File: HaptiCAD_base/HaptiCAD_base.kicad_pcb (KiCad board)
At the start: 4 copper layers, 170 x 110 mm, 99 parts, among them J101 BLDC, J301 USB_C_Receptacle_USB2.0_16P, J801 SWD, J802 Micro_SD_Card, U201 SN74LV1T34DBV, U401 MT6701CT, U402 VEML7700-TT, U501 AP2112K-3.3, U601 TMC6300-LA-T, U602 LMV321, U801 BMD-340-A-R, U802 ESD224DQA

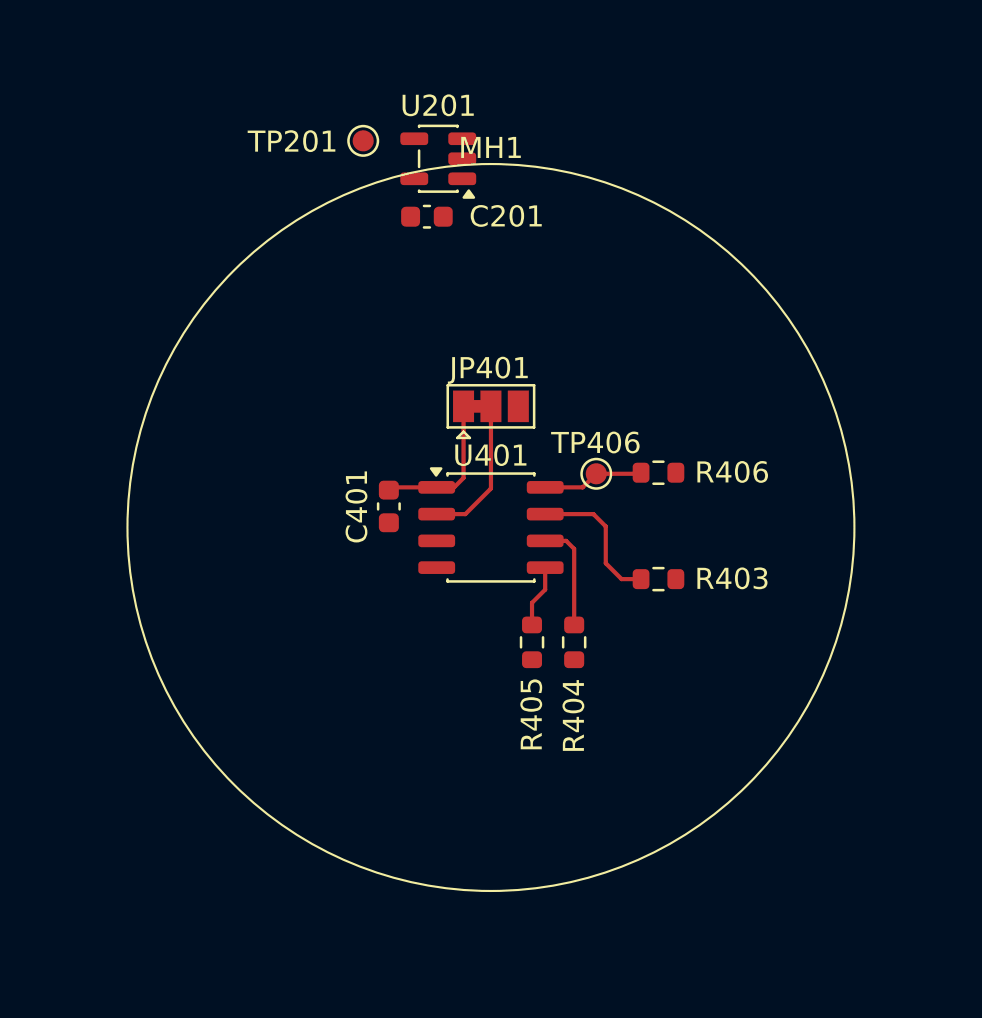
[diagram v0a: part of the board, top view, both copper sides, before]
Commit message: Split project into base and motor mount pcb
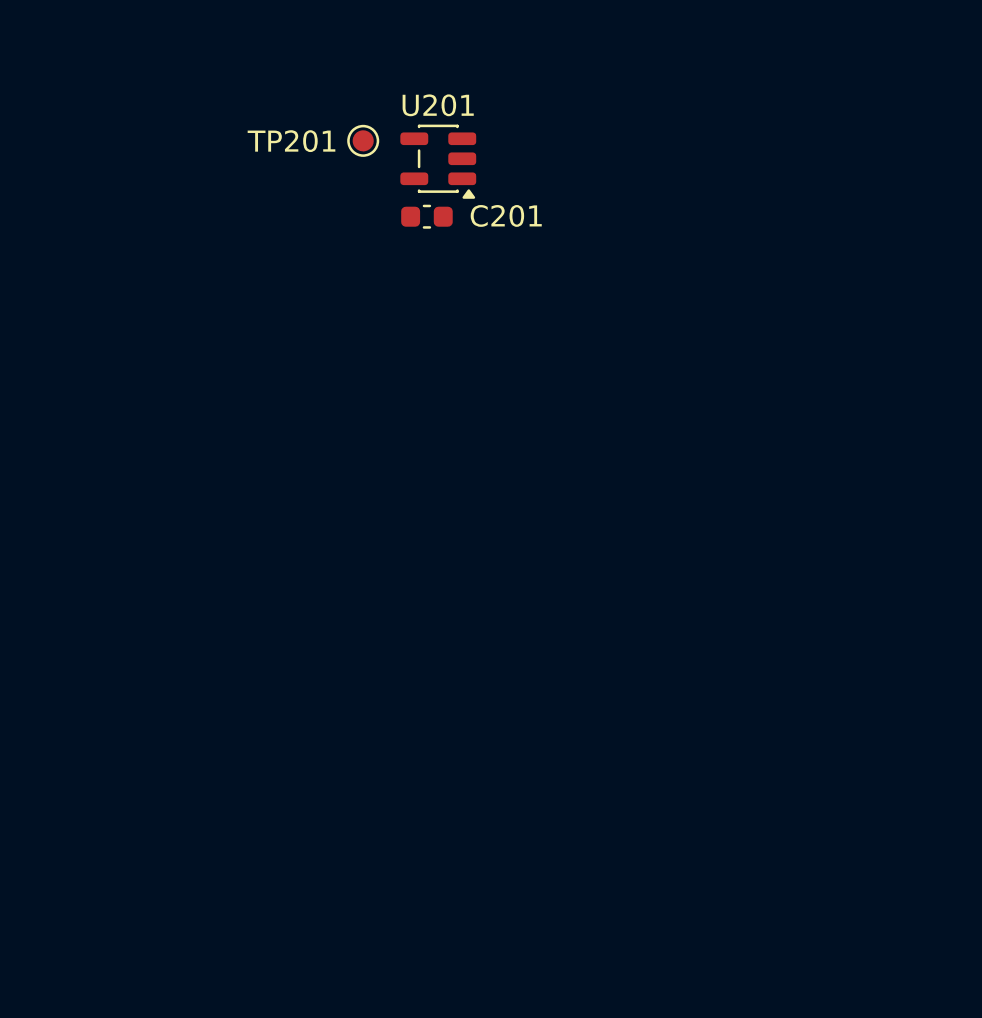
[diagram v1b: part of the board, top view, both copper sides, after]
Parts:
- removed C401: 0.1uF, Capacitor_SMD:C_0603_1608Metric
- removed JP401: SolderJumper_3_Bridged12, Jumper:SolderJumper-3_P1.3mm_Bridged12_Pad1.0x1.5mm
- removed MH1: ~, BLDC_mount:BLDC_mount
- removed R403, R404: 2.2k, Resistor_SMD:R_0603_1608Metric
- removed R405: 100k, Resistor_SMD:R_0603_1608Metric
- removed R406: 0, Resistor_SMD:R_0603_1608Metric
- removed TP406: ENC__~{CS}, TestPoint:TestPoint_Pad_D1.0mm
- removed U401: MT6701CT, Package_SO:SO-8_3.9x4.9mm_P1.27mm
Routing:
- net 5V: track 24.4 -> 17.2 mm
- net Net-(JP401-C): track 6.98 -> 0.00 mm
- net /Sensors/ENC_CLK: track 6.85 -> 0.00 mm
- net /Sensors/ENC_MISO: track 5.14 -> 0.00 mm
- net /Sensors/ENC__~{CS}: track 4.89 -> 0.00 mm
- net /Sensors/ENC__PUSH: track 2.98 -> 0.00 mm

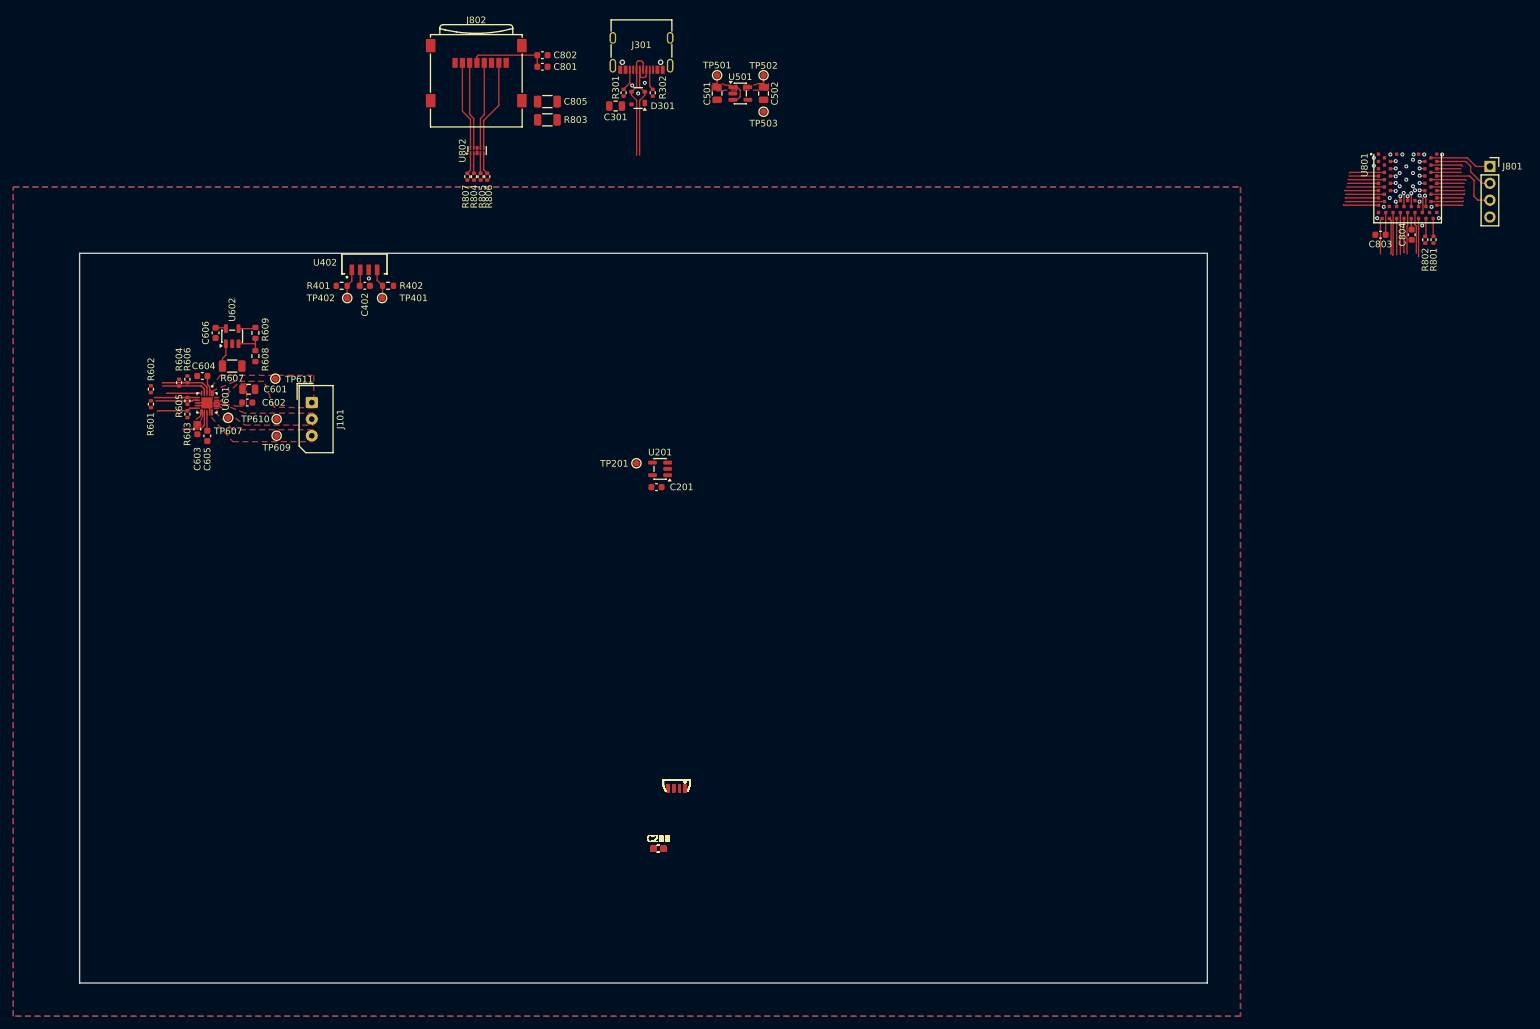
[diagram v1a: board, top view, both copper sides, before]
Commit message: updated base schematic and PCB
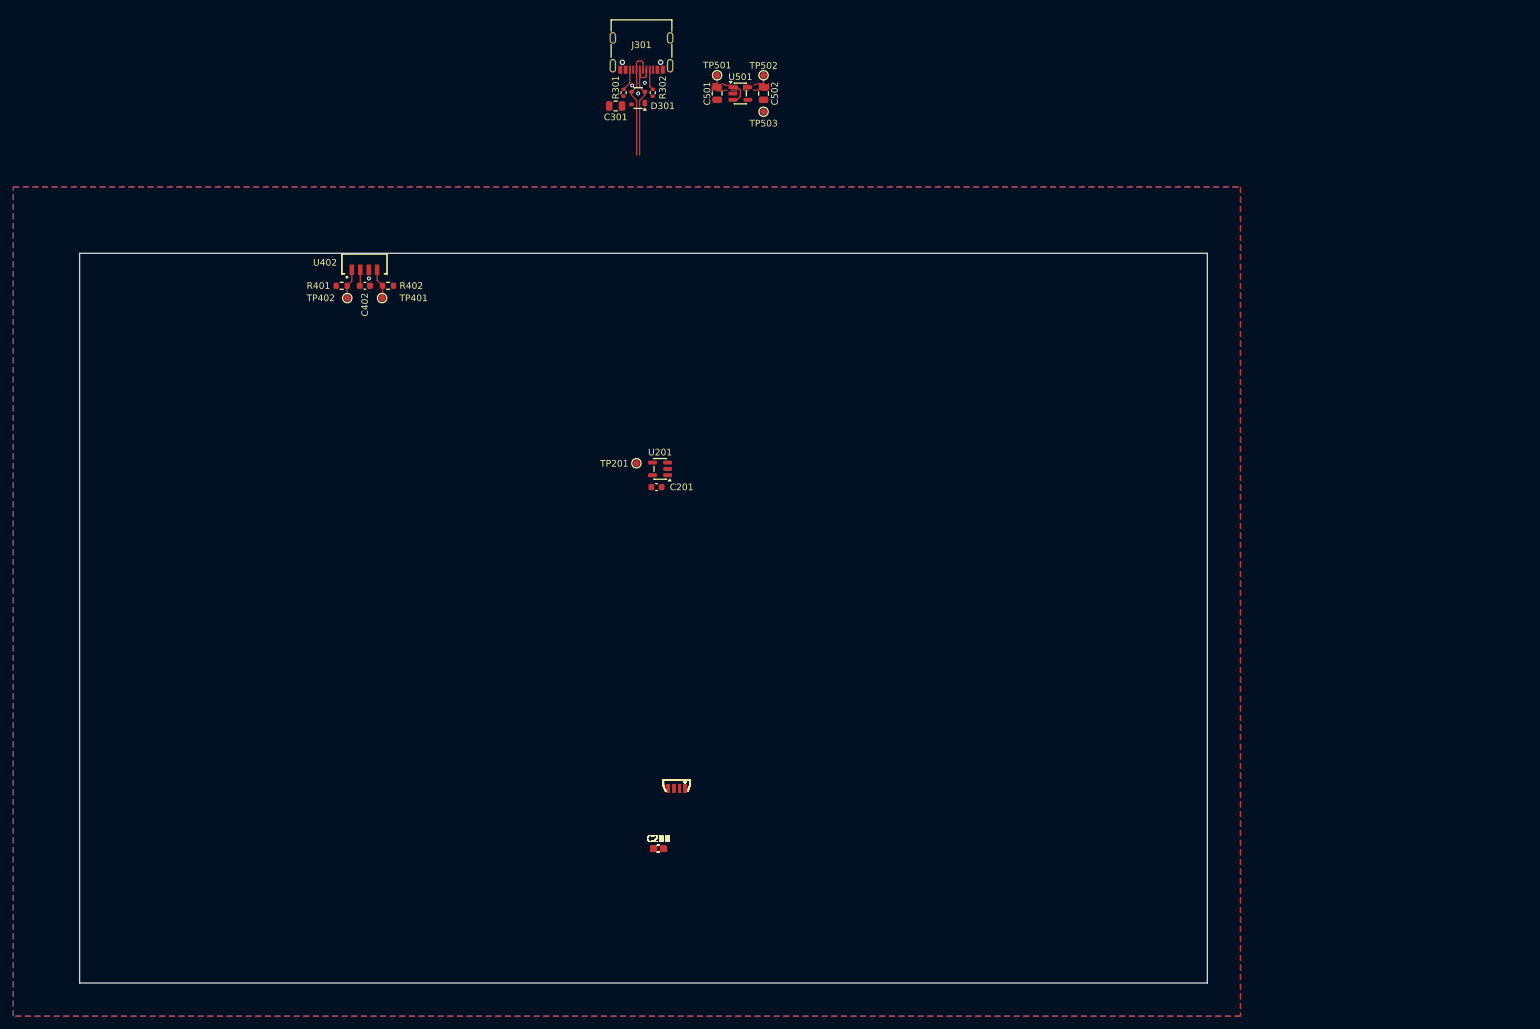
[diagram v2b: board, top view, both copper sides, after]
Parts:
- removed C601: 10uF, Capacitor_SMD:C_0805_2012Metric
- removed C602, C603, C604, C605, C606: 0.1nF, Capacitor_SMD:C_0603_1608Metric
- removed C801: 10uF, Capacitor_SMD:C_0603_1608Metric
- removed C802: 0.1uF, Capacitor_SMD:C_0603_1608Metric
- removed C803, C804: 4.7uF, Capacitor_SMD:C_0603_1608Metric
- removed C805: 2.2uF, Capacitor_SMD:C_1206_3216Metric
- removed J101: BLDC, Connector_Molex:Molex_SPOX_5267-03A_1x03_P2.50mm_Vertical
- removed J801: SWD, Connector_PinSocket_2.54mm:PinSocket_1x04_P2.54mm_Vertical
- removed J802: Micro_SD_Card, Connector_Card:microSD_HC_Wuerth_693072010801
- removed R601, R602, R603, R604, R605, R606, R804, R805, R806, R807: 100k, Resistor_SMD:R_0402_1005Metric
- removed R607: 150m, Resistor_SMD:R_1206_3216Metric
- removed R608: 2k, Resistor_SMD:R_0603_1608Metric
- removed R609: 18k, Resistor_SMD:R_0603_1608Metric
- removed R801, R802: 27, Resistor_SMD:R_0402_1005Metric
- removed R803: 1M, Resistor_SMD:R_1206_3216Metric
- removed TP607: Cur_sens, TestPoint:TestPoint_Pad_D1.0mm
- removed TP609: MOT_U, TestPoint:TestPoint_Pad_D1.0mm
- removed TP610: MOT_V, TestPoint:TestPoint_Pad_D1.0mm
- removed TP611: MOT_W, TestPoint:TestPoint_Pad_D1.0mm
- removed U601: TMC6300-LA-T, TMC6300:QFN40P300X300X90-21N
- removed U602: LMV321, Package_TO_SOT_SMD:SOT-23-5
- removed U801: BMD-340-A-R, BMD-340-A-R:RIGADO_BMD-340-A-R
- removed U802: ESD224DQA, Package_DFN_QFN:Diodes_UDFN-10_1x2.5mm_P0.5mm
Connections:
- net /Sensors/SCL renamed /MCU/I2C1_SCL
- net /Sensors/SDA renamed /MCU/I2C1_SDA
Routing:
- net 3.3V: track 19.5 -> 4.24 mm
- net Net-(J802-DAT0): track 13.8 -> 0.00 mm
- net Net-(J802-DAT3/CD): track 13.2 -> 0.00 mm
- net Net-(J802-CMD): track 13.1 -> 0.00 mm
- net Net-(J802-CLK): track 13.0 -> 0.00 mm
- net 5V: track 17.2 -> 5.43 mm
- net /MCU/~{RESET}: track 10.9 -> 0.00 mm
- net /MCU/SW_CLK: track 9.84 -> 0.00 mm
- net /MCU/SW_DIO: track 9.44 -> 0.00 mm
- net /Motor driver/MOT_UH: track 7.89 -> 0.00 mm
- net /Motor driver/MOT_VH: track 7.12 -> 0.00 mm
- net /MCU/P0.03: track 6.49 -> 0.00 mm
- net /Motor driver/MOT_UL: track 6.49 -> 0.00 mm
- net /MCU/P0.05: track 6.35 -> 0.00 mm
- net /MCU/P0.07: track 6.29 -> 0.00 mm
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- removed copper zone on F.Cu, net /Motor driver/MOT_U
- removed copper zone on F.Cu, net /Motor driver/MOT_V
- removed copper zone on F.Cu, net /Motor driver/MOT_W
